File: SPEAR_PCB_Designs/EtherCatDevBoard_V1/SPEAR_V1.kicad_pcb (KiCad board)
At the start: 4 copper layers, 55.8 x 39 mm, 32 parts, among them J2 USB_C_Receptacle_USB2.0_16P, J3 Conn_01x21_Pin, J5 Conn_01x21_Pin, J6 FTSH-107-01-F-DV-K-P-TR, SW1 SW_Push, U1 STM32F446RCTx, U2 USBLC6-2SC6, U3 AMS1117-3.3, Y1 16MHz

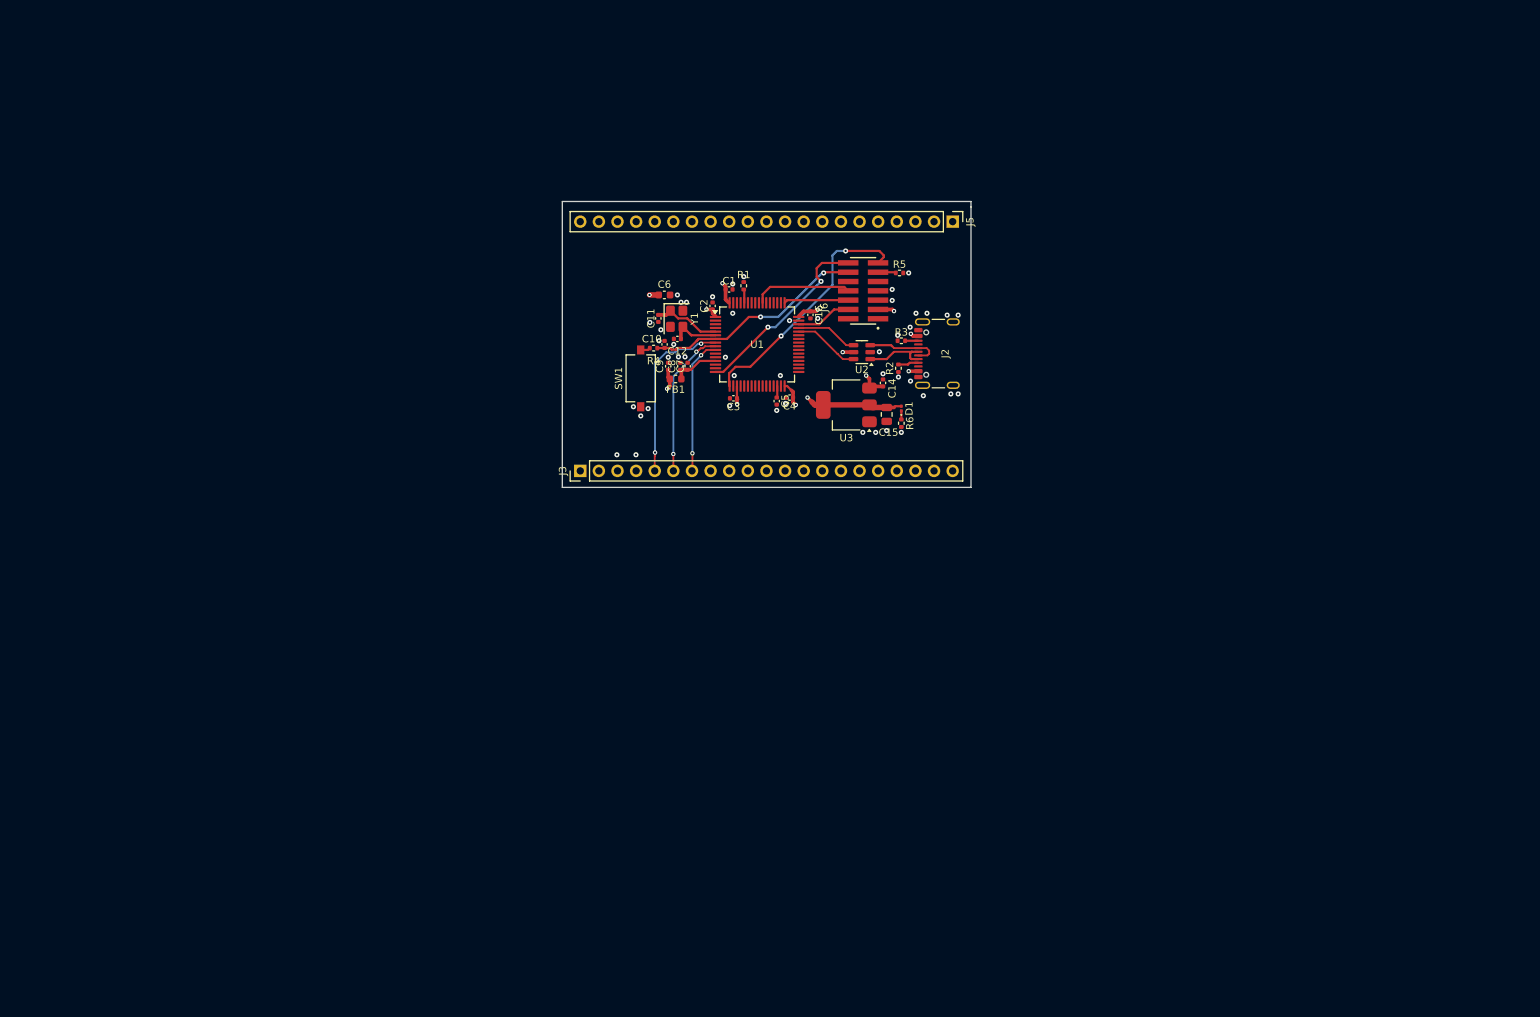
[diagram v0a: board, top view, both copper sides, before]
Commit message: Added Lan9252 EtherCAT system to the microcontroller dev board. The schematic is updated, but the pcb layout is still being worked on.
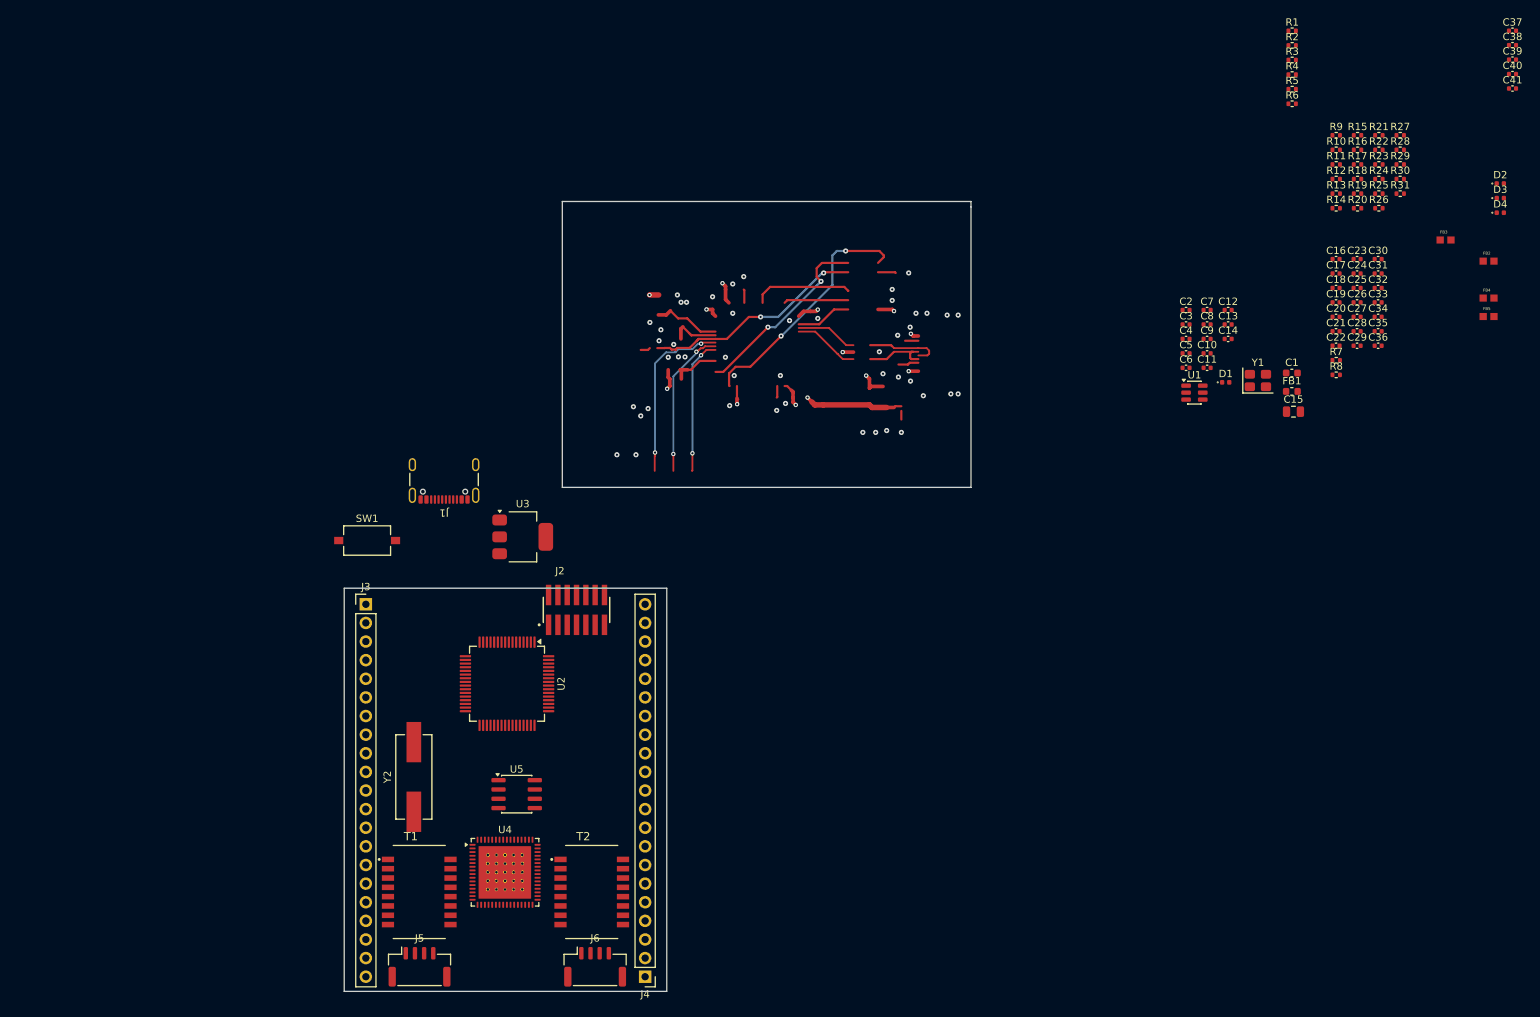
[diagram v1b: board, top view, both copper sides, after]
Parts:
- added C13: 2.2u, Capacitor_SMD:C_0402_1005Metric, F.Cu at (198.6, 66.0)
- added C17: 0.1uF, Capacitor_SMD:C_0402_1005Metric, F.Cu at (213.3, 59.1)
- added C18: 1uF, Capacitor_SMD:C_0402_1005Metric, F.Cu at (213.3, 61.0)
- added C19: 0.1uF, Capacitor_SMD:C_0402_1005Metric, F.Cu at (213.3, 63.0)
- added C20: 0.1uF, Capacitor_SMD:C_0402_1005Metric, F.Cu at (213.3, 65.0)
- added C21: 0.1uF, Capacitor_SMD:C_0402_1005Metric, F.Cu at (213.3, 67.0)
- added C22: 0.1uF, Capacitor_SMD:C_0402_1005Metric, F.Cu at (213.3, 68.9)
- added C23: 0.1uF, Capacitor_SMD:C_0402_1005Metric, F.Cu at (216.2, 57.1)
- added C24: 0.1uF, Capacitor_SMD:C_0402_1005Metric, F.Cu at (216.2, 59.1)
- added C25: 0.1uF, Capacitor_SMD:C_0402_1005Metric, F.Cu at (216.2, 61.0)
- added C26: 0.1uF, Capacitor_SMD:C_0402_1005Metric, F.Cu at (216.2, 63.0)
- added C27: 0.1uF, Capacitor_SMD:C_0402_1005Metric, F.Cu at (216.2, 65.0)
- added C28: 0.1uF, Capacitor_SMD:C_0402_1005Metric, F.Cu at (216.2, 67.0)
- added C29: 0.1uF, Capacitor_SMD:C_0402_1005Metric, F.Cu at (216.2, 68.9)
- added C30: 0.1uF, Capacitor_SMD:C_0402_1005Metric, F.Cu at (219.0, 57.1)
- added C31: 18pF, Capacitor_SMD:C_0402_1005Metric, F.Cu at (219.0, 59.1)
- added C32: 18pF, Capacitor_SMD:C_0402_1005Metric, F.Cu at (219.0, 61.0)
- added C33: 0.1uF, Capacitor_SMD:C_0402_1005Metric, F.Cu at (219.0, 63.0)
- added C34: 0.1uF, Capacitor_SMD:C_0402_1005Metric, F.Cu at (219.0, 65.0)
- added C35: 0.1uF, Capacitor_SMD:C_0402_1005Metric, F.Cu at (219.0, 67.0)
- added C36: 0.1uF, Capacitor_SMD:C_0402_1005Metric, F.Cu at (219.0, 68.9)
- added C37: 1000 uF, Capacitor_SMD:C_0402_1005Metric, F.Cu at (237.4, 26.0)
- added C38: C, Capacitor_SMD:C_0402_1005Metric, F.Cu at (237.4, 27.9)
- added C39: 0.1 uF, Capacitor_SMD:C_0402_1005Metric, F.Cu at (237.4, 29.9)
- added C40: 1000 uF, Capacitor_SMD:C_0402_1005Metric, F.Cu at (237.4, 31.9)
- added C41: C, Capacitor_SMD:C_0402_1005Metric, F.Cu at (237.4, 33.8)
- added D2: LED, LED_SMD:LED_0402_1005Metric, F.Cu at (235.7, 46.8)
- added D3: LED, LED_SMD:LED_0402_1005Metric, F.Cu at (235.7, 48.8)
- added D4: LED, LED_SMD:LED_0402_1005Metric, F.Cu at (235.7, 50.8)
- added FB2: FerrriteBead, LAN9252 Footprints:Ferrite_bead, F.Cu at (234.1, 57.4)
- added FB3: FerrriteBead, LAN9252 Footprints:Ferrite_bead, F.Cu at (228.2, 54.5)
- added FB4: FerrriteBead, LAN9252 Footprints:Ferrite_bead, F.Cu at (234.1, 62.4)
- added FB5: FerrriteBead, LAN9252 Footprints:Ferrite_bead, F.Cu at (234.1, 64.9)
- added J1: USB_C_Receptacle_USB2.0_16P, Connector_USB:USB_C_Receptacle_GCT_USB4105-xx-A_16P_TopMnt_Horizontal, F.Cu at (91.6, 86.2)
- added J4: Conn_01x21_Pin, Connector_PinHeader_2.54mm:PinHeader_1x21_P2.54mm_Vertical, F.Cu at (119.0, 155.0)
- added R10: 1k, Resistor_SMD:R_0402_1005Metric, F.Cu at (213.3, 42.2)
- added R11: 49.9 R, Resistor_SMD:R_0402_1005Metric, F.Cu at (213.3, 44.2)
- added R12: 49.9 R, Resistor_SMD:R_0402_1005Metric, F.Cu at (213.3, 46.2)
- added R13: 49.9 R, Resistor_SMD:R_0402_1005Metric, F.Cu at (213.3, 48.2)
- added R14: 49.9 R, Resistor_SMD:R_0402_1005Metric, F.Cu at (213.3, 50.2)
- added R15: 49.9 R, Resistor_SMD:R_0402_1005Metric, F.Cu at (216.2, 40.2)
- added R16: 10kR, Resistor_SMD:R_0402_1005Metric, F.Cu at (216.2, 42.2)
- added R17: 75, Resistor_SMD:R_0402_1005Metric, F.Cu at (216.2, 44.2)
- added R18: 10kR, Resistor_SMD:R_0402_1005Metric, F.Cu at (216.2, 46.2)
- added R19: 10kR, Resistor_SMD:R_0402_1005Metric, F.Cu at (216.2, 48.2)
- added R20: 75, Resistor_SMD:R_0402_1005Metric, F.Cu at (216.2, 50.2)
- added R21: 2kR, Resistor_SMD:R_0402_1005Metric, F.Cu at (219.1, 40.2)
- added R22: 2kR, Resistor_SMD:R_0402_1005Metric, F.Cu at (219.1, 42.2)
- added R23: 4.7kR, Resistor_SMD:R_0402_1005Metric, F.Cu at (219.1, 44.2)
- added R24: 1k, Resistor_SMD:R_0402_1005Metric, F.Cu at (219.1, 46.2)
- added R25: 49.9 R, Resistor_SMD:R_0402_1005Metric, F.Cu at (219.1, 48.2)
- added R26: 49.9 R, Resistor_SMD:R_0402_1005Metric, F.Cu at (219.1, 50.2)
- added R27: 49.9 R, Resistor_SMD:R_0402_1005Metric, F.Cu at (222.1, 40.2)
- added R28: 49.9 R, Resistor_SMD:R_0402_1005Metric, F.Cu at (222.1, 42.2)
- added R29: 49.9 R, Resistor_SMD:R_0402_1005Metric, F.Cu at (222.1, 44.2)
- added R30: 75, Resistor_SMD:R_0402_1005Metric, F.Cu at (222.1, 46.2)
- added R31: 75, Resistor_SMD:R_0402_1005Metric, F.Cu at (222.1, 48.2)
- added R7: 0R, Resistor_SMD:R_0402_1005Metric, F.Cu at (213.3, 70.9)
- added R8: 12.1k, Resistor_SMD:R_0402_1005Metric, F.Cu at (213.3, 72.9)
- added R9: 270R, Resistor_SMD:R_0402_1005Metric, F.Cu at (213.3, 40.2)
- added T1: H1102NLT, LAN9252 Footprints:XFMR_H1102NLT, F.Cu at (88.2, 143.4)
- added T2: H1102NLT, LAN9252 Footprints:XFMR_H1102NLT, F.Cu at (111.8, 143.4)
- added U4: LAN9252I/ML, LAN9252 Footprints:LAN9252_QFN UPDATED, F.Cu at (99.9, 140.8)
- added U5: 24FC512, Package_SO:SOIC-8_3.9x4.9mm_P1.27mm, F.Cu at (101.5, 130.1)
- added Y2: 25MHz, LAN9252 Footprints:Y_Wurth_WE-XTAL_Quartz-HC49-4HSMX, F.Cu at (87.5, 127.8)
- C1: value 100n -> 10u; footprint Capacitor_SMD:C_0402_1005Metric -> Capacitor_SMD:C_0603_1608Metric
- C16: value 100n -> 1uF
- C5: value 2.2u -> 100n
- C6: value 10u -> 100n; footprint Capacitor_SMD:C_0603_1608Metric -> Capacitor_SMD:C_0402_1005Metric
- D1: footprint LED_SMD:LED_0201_0603Metric -> LED_SMD:LED_0402_1005Metric
- J2: value USB_C_Receptacle_USB2.0_16P -> FTSH-107-01-F-DV-K-P-TR; footprint Connector_USB:USB_C_Receptacle_GCT_USB4105-xx-A_16P_TopMnt_Horizontal -> LAN9252 Footprints:SAMTEC_FTSH-107-01-F-DV-K-P-TR
- J5: value Conn_01x21_Pin -> SM04B-GHS-TB; footprint Connector_PinHeader_2.54mm:PinHeader_1x21_P2.54mm_Vertical -> Connector_JST:JST_GH_SM04B-GHS-TB_1x04-1MP_P1.25mm_Horizontal
- J6: value FTSH-107-01-F-DV-K-P-TR -> SM04B-GHS-TB; footprint Library:SAMTEC_FTSH-107-01-F-DV-K-P-TR -> Connector_JST:JST_GH_SM04B-GHS-TB_1x04-1MP_P1.25mm_Horizontal
- R1: value 10k -> 100R
- R2: value 5.1k -> 10k
- R4: value 100R -> 5.1k
- U1: value STM32F446RCTx -> USBLC6-2SC6; footprint Package_QFP:LQFP-64_10x10mm_P0.5mm -> Package_TO_SOT_SMD:SOT-23-6
- U2: value USBLC6-2SC6 -> STM32F446RCT6; footprint Package_TO_SOT_SMD:SOT-23-6 -> Package_QFP:LQFP-64_10x10mm_P0.5mm
- moved J5 125.0 mm to (88.3, 153.7), turned to 0 degrees
- moved J6 99.2 mm to (112.2, 153.7), turned to 0 degrees
- moved R4 94.8 mm to (207.3, 31.9), turned to 0 degrees
- moved FB1 84.1 mm to (207.3, 75.2), turned to 0 degrees
- moved R1 82.5 mm to (207.3, 26.0), turned to 0 degrees
- moved Y1 79.7 mm to (202.6, 73.7), turned to 0 degrees
- moved C1 77.6 mm to (207.3, 72.7)
- moved C12 75.2 mm to (198.6, 64.1), turned to 0 degrees
- moved C11 75.2 mm to (195.7, 71.9), turned to 0 degrees
- moved C10 74.0 mm to (195.7, 70.0), turned to 0 degrees
- moved C9 73.6 mm to (195.7, 68.0), turned to 0 degrees
- moved C16 72.1 mm to (213.3, 57.1), turned to 0 degrees
- moved C8 72.1 mm to (195.7, 66.0), turned to 0 degrees
- moved C6 71.9 mm to (192.8, 71.9)
- moved C7 71.3 mm to (195.7, 64.1), turned to 0 degrees
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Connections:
- net /PWR_LED_K renamed /STM32F446RC/PWR_LED_K
- C10 pad 1: /NRST -> /STM32F446RC/NRST
- C11 pad 1: /HSE_IN -> /STM32F446RC/HSE_OUT
- C12 pad 1: /HSE_OUT -> /STM32F446RC/HSE_IN
- C16 pad 1: +3.3V -> /LAN9252/VDD33TXRX1
- C16 pad 2: GND -> Net-(C16-Pad2)
- C5 pad 1: Net-(U1-VCAP_1) -> +3.3V
- J3 pad 10: /PA1 -> /STM32F446RC/PA1
- J3 pad 11: /PA4 -> /STM32F446RC/PA4
- J3 pad 12: /PC4 -> /STM32F446RC/PC4
- J3 pad 13: /PC5 -> /STM32F446RC/PC5
- J3 pad 14: /PB0 -> /STM32F446RC/PB0
- J3 pad 15: /PB1 -> /STM32F446RC/PB1
- J3 pad 16: /PB2 -> /STM32F446RC/PB2
- J3 pad 17: /PB10 -> /STM32F446RC/PB10
- J3 pad 18: /PB12 -> /STM32F446RC/PB12
- J3 pad 19: /PB13 -> /STM32F446RC/PB13
- J3 pad 20: /PB14 -> /STM32F446RC/PB14
- J3 pad 21: /PB15 -> /STM32F446RC/PB15
- J3 pad 5: /PC0 -> /STM32F446RC/PC0
- J3 pad 6: /PC1 -> /STM32F446RC/PC1
- J3 pad 7: /PC2 -> /STM32F446RC/PC2
- J3 pad 8: /PC3 -> /STM32F446RC/PC3
- J3 pad 9: /PA0 -> /STM32F446RC/PA0
- J5 pad 1: /PC6 -> Net-(J5-Pin_1)
- J5 pad 2: /PC7 -> Net-(J5-Pin_2)
- J5 pad 3: /PC8 -> Net-(J5-Pin_3)
- J5 pad 4: /PC9 -> Net-(J5-Pin_4)
- R1 pad 1: /BOOT0 -> /STM32F446RC/NRST
- R1 pad 2: GND -> Net-(R1-Pad2)
- R2 pad 1: GND -> /STM32F446RC/BOOT0
- R2 pad 2: Net-(J2-CC1) -> GND
- R3 pad 2: Net-(J2-CC2) -> Net-(J1-CC1)
- R4 pad 1: /NRST -> GND
- R4 pad 2: Net-(R4-Pad2) -> Net-(J1-CC2)
- R5 pad 1: Net-(J6-Pad11) -> Net-(J2-Pad11)
- SW1 pad 2: Net-(R4-Pad2) -> Net-(R1-Pad2)
- U1 pad 1: +3.3V -> /STM32F446RC/USBC_D-
- U1 pad 2: /PC13 -> GND
- U1 pad 3: /PC14 -> /STM32F446RC/USBC_D+
- U1 pad 4: /PC15 -> /STM32F446RC/USB_D+
- U1 pad 5: /HSE_IN -> +5V
- U1 pad 6: /HSE_OUT -> /STM32F446RC/USB_D-
- U2 pad 1: /USBC_D- -> +3.3V
- U2 pad 2: GND -> /STM32F446RC/PC13
- U2 pad 3: /USBC_D+ -> /STM32F446RC/PC14
- U2 pad 4: /USB_D+ -> /STM32F446RC/PC15
- U2 pad 5: +5V -> /STM32F446RC/HSE_IN
- U2 pad 6: /USB_D- -> /STM32F446RC/HSE_OUT
- Y1 pad 1: /HSE_IN -> /STM32F446RC/HSE_IN
- Y1 pad 3: /HSE_OUT -> /STM32F446RC/HSE_OUT
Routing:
- net (no net): track 0.00 -> 250.2 mm, vias 0 -> 12
- net /UART2_RX: track 33.8 -> 0.00 mm, vias 2 -> 0
- net /NRST: track 30.9 -> 0.00 mm, vias 2 -> 0
- net /UART2_TX: track 26.2 -> 0.00 mm, vias 2 -> 0
- net /PC0: track 24.1 -> 0.00 mm, vias 2 -> 0
- net /PC1: track 20.5 -> 0.00 mm, vias 2 -> 0
- net /PC2: track 18.6 -> 0.00 mm, vias 2 -> 0
- net /SWO: track 13.5 -> 0.00 mm
- net /USBC_D+: track 10.3 -> 0.00 mm
- net /USBC_D-: track 9.30 -> 0.00 mm
- net /HSE_IN: track 9.22 -> 0.00 mm
- net /USB_D-: track 9.03 -> 0.00 mm
- net /SWCLK: track 8.83 -> 0.00 mm
- net /USB_D+: track 8.45 -> 0.00 mm
- net /SWDIO: track 7.59 -> 0.00 mm
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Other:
- board size 55.8 x 39 mm -> 85.5 x 107.8 mm

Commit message: Continued work on the EtherCAT microcontroller dev. board. Not complete yet.
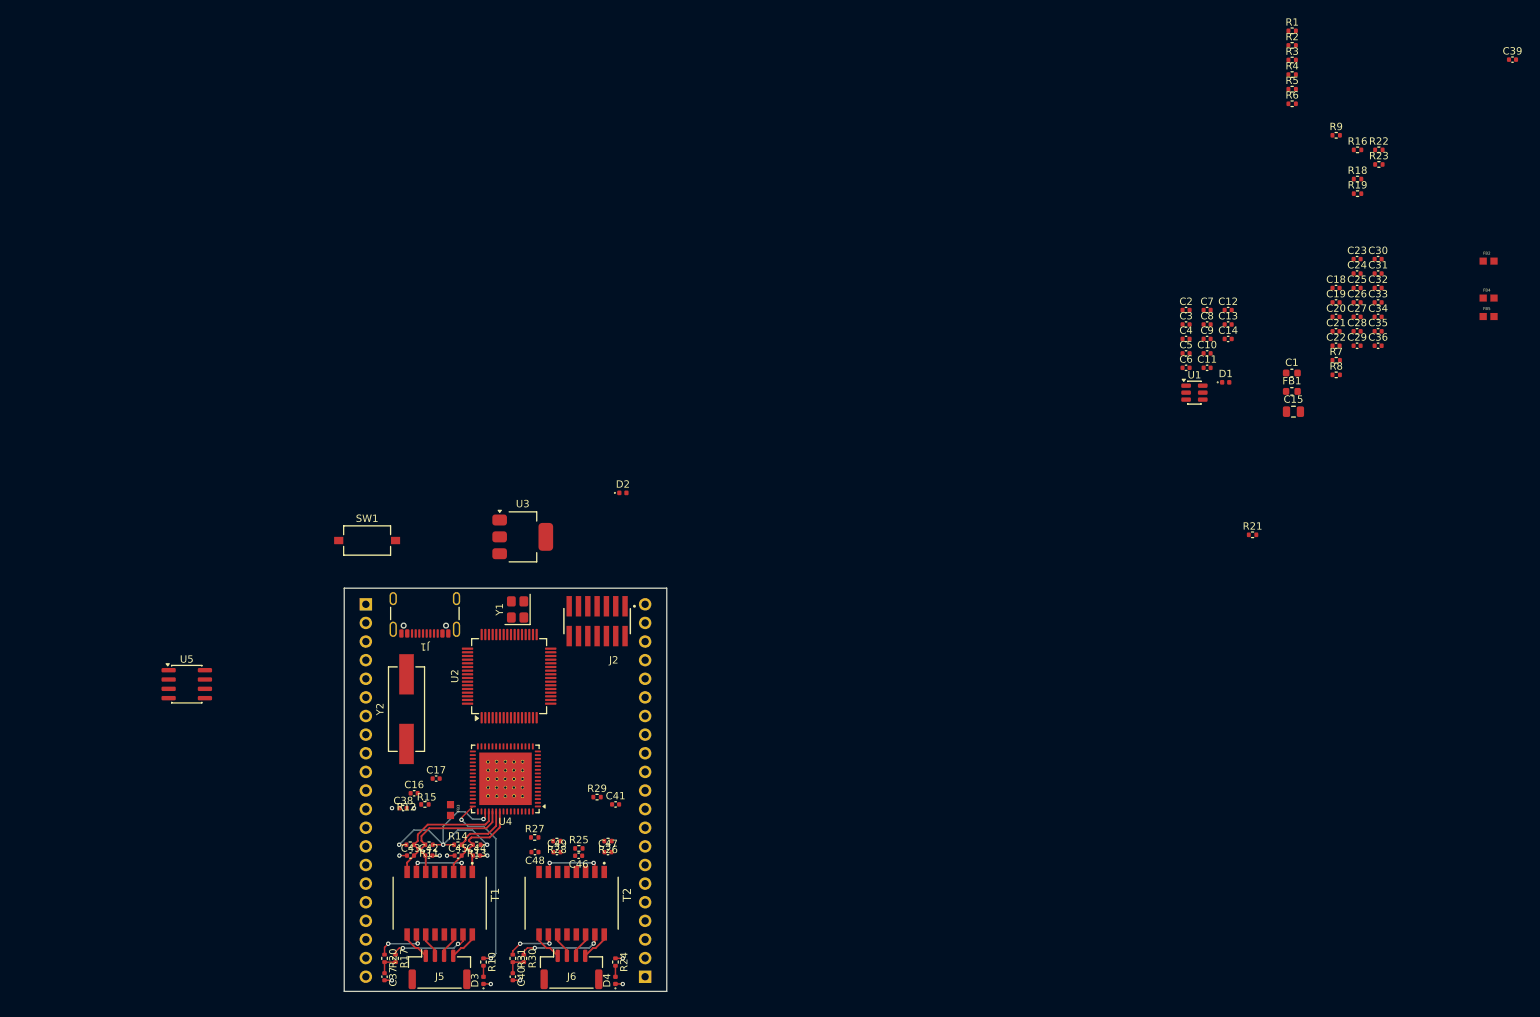
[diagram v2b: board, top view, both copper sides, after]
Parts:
- added C42: 10p, Capacitor_SMD:C_0402_1005Metric, F.Cu at (89.5, 138.5)
- added C43: 10p, Capacitor_SMD:C_0402_1005Metric, F.Cu at (87.0, 138.5)
- added C44: 10p, Capacitor_SMD:C_0402_1005Metric, F.Cu at (96.0, 138.5)
- added C45: 10p, Capacitor_SMD:C_0402_1005Metric, F.Cu at (93.5, 138.5)
- added C46: 10p, Capacitor_SMD:C_0402_1005Metric, F.Cu at (110.0, 138.5)
- added C47: 10p, Capacitor_SMD:C_0402_1005Metric, F.Cu at (114.0, 138.0)
- added C48: 10p, Capacitor_SMD:C_0402_1005Metric, F.Cu at (104.0, 138.0)
- added C49: 10p, Capacitor_SMD:C_0402_1005Metric, F.Cu at (107.0, 138.0)
- C38, C41: value C -> 22n
- FB2, FB3, FB4, FB5: value FerrriteBead -> BLM18EG221SN1D
- J3, J4: moved to B.Cu
- R11, R12, R13, R14, R25, R26, R27, R28: value 49.9 R -> 49.9R 1%
- R15, R29: value 49.9 R -> 0R
- R16, R18, R19: value 10kR -> 10k 1%
- R17, R20, R30, R31: value 75 -> 75R 1%
- R21, R22: value 2kR -> 2k 0.1%
- R8: value 12.1k -> 12.1k 1%
- U5: value 24FC512 -> 24FC512-I/SN
- moved C37 200.8 mm to (83.5, 155.0), turned to -90 degrees
- moved C40 183.7 mm to (101.0, 155.0), turned to -90 degrees
- moved C38 183.7 mm to (86.0, 132.0), turned to 180 degrees
- moved D3 175.0 mm to (97.0, 155.5), turned to 90 degrees
- moved R17 170.1 mm to (85.0, 152.5), turned to -90 degrees
- moved R20 167.6 mm to (83.5, 152.5), turned to -90 degrees
- moved R10 160.6 mm to (97.0, 153.0), turned to -90 degrees
- moved R30 160.0 mm to (102.5, 152.5), turned to -90 degrees
- moved D4 159.8 mm to (115.0, 155.5), turned to 90 degrees
- moved R31 159.8 mm to (101.0, 152.5), turned to -90 degrees
- moved R15 156.6 mm to (89.0, 131.5), turned to 180 degrees
- moved C41 156.5 mm to (115.0, 131.5)
- moved FB3 156.4 mm to (92.5, 132.3), turned to -90 degrees
- moved R12 155.6 mm to (87.0, 137.0)
- moved R11 154.7 mm to (89.6, 137.0), turned to 180 degrees
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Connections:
- C24 pad 1: +3.3V -> Net-(U4-VDD33BIAS)
- J5 pad 1: Net-(J5-Pin_1) -> /LAN9252/LAN9252 Ports/TXA+
- J5 pad 2: Net-(J5-Pin_2) -> /LAN9252/LAN9252 Ports/TXA-
- J5 pad 3: Net-(J5-Pin_3) -> /LAN9252/LAN9252 Ports/RXA+
- J5 pad 4: Net-(J5-Pin_4) -> /LAN9252/LAN9252 Ports/RXA-
- J6 pad 1: Net-(J6-Pin_1) -> /LAN9252/LAN9252 Ports/TXB+
- J6 pad 2: Net-(J6-Pin_2) -> /LAN9252/LAN9252 Ports/TXB-
- J6 pad 3: Net-(J6-Pin_3) -> /LAN9252/LAN9252 Ports/RXB+
- J6 pad 4: Net-(J6-Pin_4) -> /LAN9252/LAN9252 Ports/RXB-
- T1 pad 1: /LAN9252/TXA_P -> /LAN9252/RXA_P
- T1 pad 11: Net-(J5-Pin_3) -> /LAN9252/LAN9252 Ports/TXA-
- T1 pad 14: Net-(J5-Pin_2) -> /LAN9252/LAN9252 Ports/RXA+
- T1 pad 16: Net-(J5-Pin_1) -> /LAN9252/LAN9252 Ports/RXA-
- T1 pad 3: /LAN9252/TXA_N -> /LAN9252/RXA_N
- T1 pad 6: /LAN9252/RXA_P -> /LAN9252/TXA_P
- T1 pad 8: /LAN9252/RXA_N -> /LAN9252/TXA_N
- T1 pad 9: Net-(J5-Pin_4) -> /LAN9252/LAN9252 Ports/TXA+
- T2 pad 1: /LAN9252/TXB_P -> /LAN9252/TXB_N
- T2 pad 11: Net-(J6-Pin_3) -> /LAN9252/LAN9252 Ports/TXB-
- T2 pad 14: Net-(J6-Pin_2) -> /LAN9252/LAN9252 Ports/RXB+
- T2 pad 16: Net-(J6-Pin_1) -> /LAN9252/LAN9252 Ports/RXB-
- T2 pad 3: /LAN9252/TXB_N -> /LAN9252/TXB_P
- T2 pad 6: /LAN9252/RXB_P -> /LAN9252/RXB_N
- T2 pad 8: /LAN9252/RXB_N -> /LAN9252/RXB_P
- T2 pad 9: Net-(J6-Pin_4) -> /LAN9252/LAN9252 Ports/TXB+
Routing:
- net (no net): track 250.2 -> 0.00 mm, vias 12 -> 0
- net +3.3V: track 33.8 -> 0.00 mm, vias 9 -> 0
- net /LAN9252/VDD33TXRX1: track 0.00 -> 30.5 mm, vias 0 -> 4
- net /LAN9252/GPIO0: track 0.00 -> 25.8 mm, vias 0 -> 2
- net /LAN9252/TXA_N: track 0.00 -> 17.9 mm
- net /LAN9252/TXA_P: track 0.00 -> 17.5 mm
- net /LAN9252/RXA_N: track 0.00 -> 12.5 mm
- net /LAN9252/RXA_P: track 0.00 -> 12.2 mm
- net Net-(R30-Pad1): track 0.00 -> 11.7 mm, vias 0 -> 2
- net Net-(R17-Pad1): track 0.00 -> 11.1 mm, vias 0 -> 2
- net Net-(C38-Pad1): track 0.00 -> 8.62 mm, vias 0 -> 3
- net Net-(C41-Pad1): track 0.00 -> 8.61 mm, vias 0 -> 2
- net GND: track 0.00 -> 8.11 mm, vias 47 -> 9
- net +5V: track 7.77 -> 0.00 mm, vias 4 -> 0
- net Net-(R31-Pad1): track 0.00 -> 7.21 mm, vias 0 -> 2
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- removed copper zone on In2.Cu, net +5V
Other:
- board size 85.5 x 107.8 mm -> 44 x 55 mm
